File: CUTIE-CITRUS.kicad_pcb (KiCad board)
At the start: 2 copper layers, 85 x 85 mm, 65 parts, among them J1 F32Q-1A7H1-11022, J2 F32Q-1A7H1-11022, J3 Bus_M.2_Socket_M, J4 Hirose U.FL, U1 AP3441SHE-7B, U2 ASEK-32.768KHZ-L-R-T, U3 ICM-42688-P, U4 NEO-M8M

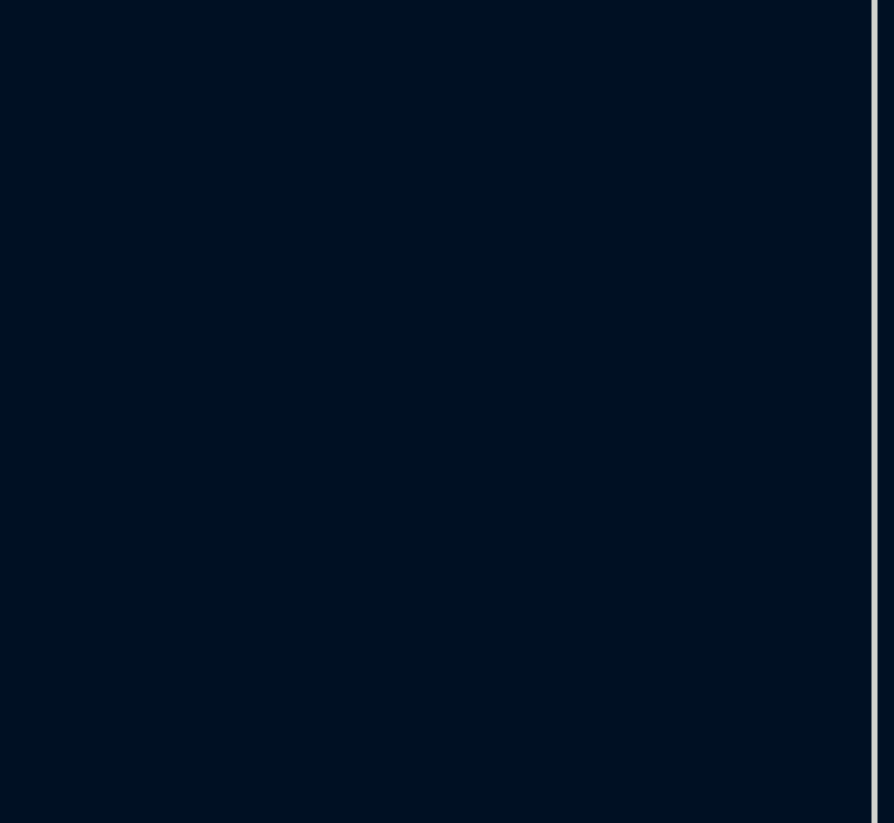
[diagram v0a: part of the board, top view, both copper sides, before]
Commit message: moved TPs
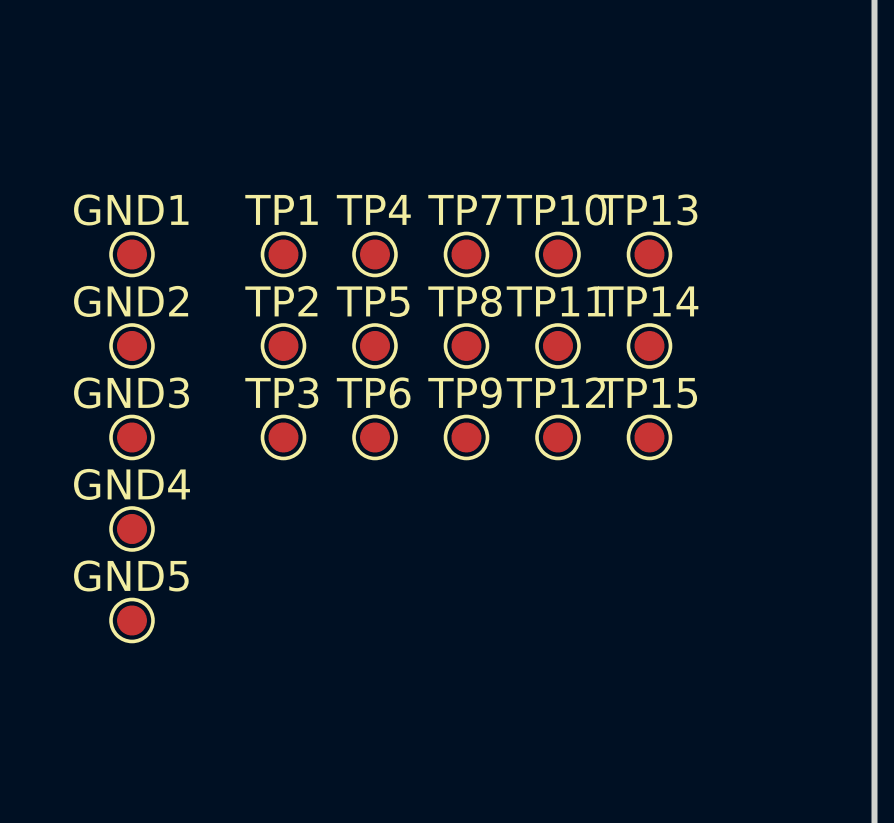
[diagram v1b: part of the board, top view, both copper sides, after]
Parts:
- added GND1: TestPoint, TestPoint:TestPoint_Pad_D1.0mm, F.Cu at (125.2, 96.4)
- added GND2: TestPoint, TestPoint:TestPoint_Pad_D1.0mm, F.Cu at (125.2, 99.5)
- added GND3: TestPoint, TestPoint:TestPoint_Pad_D1.0mm, F.Cu at (125.2, 102.5)
- added GND4: TestPoint, TestPoint:TestPoint_Pad_D1.0mm, F.Cu at (125.2, 105.5)
- added GND5: TestPoint, TestPoint:TestPoint_Pad_D1.0mm, F.Cu at (125.2, 108.6)
- added TP1: TestPoint, TestPoint:TestPoint_Pad_D1.0mm, F.Cu at (130.3, 96.4)
- added TP10: TestPoint, TestPoint:TestPoint_Pad_D1.0mm, F.Cu at (139.4, 96.4)
- added TP11: TestPoint, TestPoint:TestPoint_Pad_D1.0mm, F.Cu at (139.4, 99.5)
- added TP12: TestPoint, TestPoint:TestPoint_Pad_D1.0mm, F.Cu at (139.4, 102.5)
- added TP13: TestPoint, TestPoint:TestPoint_Pad_D1.0mm, F.Cu at (142.5, 96.4)
- added TP14: TestPoint, TestPoint:TestPoint_Pad_D1.0mm, F.Cu at (142.5, 99.5)
- added TP15: TestPoint, TestPoint:TestPoint_Pad_D1.0mm, F.Cu at (142.5, 102.5)
- added TP2: TestPoint, TestPoint:TestPoint_Pad_D1.0mm, F.Cu at (130.3, 99.5)
- added TP3: TestPoint, TestPoint:TestPoint_Pad_D1.0mm, F.Cu at (130.3, 102.5)
- added TP4: TestPoint, TestPoint:TestPoint_Pad_D1.0mm, F.Cu at (133.3, 96.4)
- added TP5: TestPoint, TestPoint:TestPoint_Pad_D1.0mm, F.Cu at (133.3, 99.5)
- added TP6: TestPoint, TestPoint:TestPoint_Pad_D1.0mm, F.Cu at (133.3, 102.5)
- added TP7: TestPoint, TestPoint:TestPoint_Pad_D1.0mm, F.Cu at (136.4, 96.4)
- added TP8: TestPoint, TestPoint:TestPoint_Pad_D1.0mm, F.Cu at (136.4, 99.5)
- added TP9: TestPoint, TestPoint:TestPoint_Pad_D1.0mm, F.Cu at (136.4, 102.5)
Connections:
- net /Sensors/RF_UBLOX renamed /Sensors/RF_GPS
- CM5-1 pad 102: /PCIEsb.nCLKREQ -> /CM5/PCIEsb.nCLKREQ
- CM5-1 pad 104: /PCIEsb.nWAKE -> /CM5/PCIEsb.nWAKE
- CM5-1 pad 106: /PCIEsb.PWR_EN -> /CM5/PCIEsb.PWR_EN
- CM5-1 pad 109: /PCIEsb.nRST -> /CM5/PCIEsb.nRST
- CM5-1 pad 34: /I2C2.SCL -> /CM5/I2C2.SCL
- CM5-1 pad 35: /I2C1.SCL -> /CM5/I2C1.SCL
- CM5-1 pad 36: /I2C1.SDA -> /CM5/I2C1.SDA
- CM5-1 pad 37: /SPI0.CS1n -> /CM5/SPI0.CS1n
- CM5-1 pad 38: /SPI0.SCLK -> /CM5/SPI0.SCLK
- CM5-1 pad 39: /SPI0.CS0n -> /CM5/SPI0.CS0n
- CM5-1 pad 40: /SPI0.MISO -> /CM5/SPI0.MISO
- CM5-1 pad 44: /SPI0.MOSI -> /CM5/SPI0.MOSI
- CM5-1 pad 54: /I2C2.SDA -> /CM5/I2C2.SDA
- CM5-1 pad 80: /I2C0.SCL -> /CM5/I2C0.SCL
- CM5-1 pad 82: /I2C0.SDA -> /CM5/I2C0.SDA
- J1 pad 20: /I2C0.SCL -> /CM5/I2C0.SCL
- J1 pad 21: /I2C0.SDA -> /CM5/I2C0.SDA
- J2 pad 20: /I2C1.SCL -> /CM5/I2C1.SCL
- J2 pad 21: /I2C1.SDA -> /CM5/I2C1.SDA
- J3 pad 50: /PCIEsb.nRST -> /CM5/PCIEsb.nRST
- J3 pad 52: /PCIEsb.nCLKREQ -> /CM5/PCIEsb.nCLKREQ
- J3 pad 54: /PCIEsb.nWAKE -> /CM5/PCIEsb.nWAKE
- R1 pad 2: /I2C1.SDA -> /CM5/I2C1.SDA
- R10 pad 2: /I2C2.SCL -> /CM5/I2C2.SCL
- R11 pad 2: /I2C0.SDA -> /CM5/I2C0.SDA
- R12 pad 2: /I2C0.SCL -> /CM5/I2C0.SCL
- R2 pad 2: /I2C1.SCL -> /CM5/I2C1.SCL
- R5 pad 1: /PCIEsb.PWR_EN -> /CM5/PCIEsb.PWR_EN
- R9 pad 2: /I2C2.SDA -> /CM5/I2C2.SDA
- U1 pad 7: /PCIEsb.PWR_EN -> /CM5/PCIEsb.PWR_EN
- U3 pad 1: /SPI0.MISO -> /CM5/SPI0.MISO
- U3 pad 12: /SPI0.CS0n -> /CM5/SPI0.CS0n
- U3 pad 13: /SPI0.SCLK -> /CM5/SPI0.SCLK
- U3 pad 14: /SPI0.MOSI -> /CM5/SPI0.MOSI
- U4 pad 18: /SPI0.CS1n -> /CM5/SPI0.CS1n
- U4 pad 19: /SPI0.SCLK -> /CM5/SPI0.SCLK
- U4 pad 20: /SPI0.MISO -> /CM5/SPI0.MISO
- U4 pad 21: /SPI0.MOSI -> /CM5/SPI0.MOSI

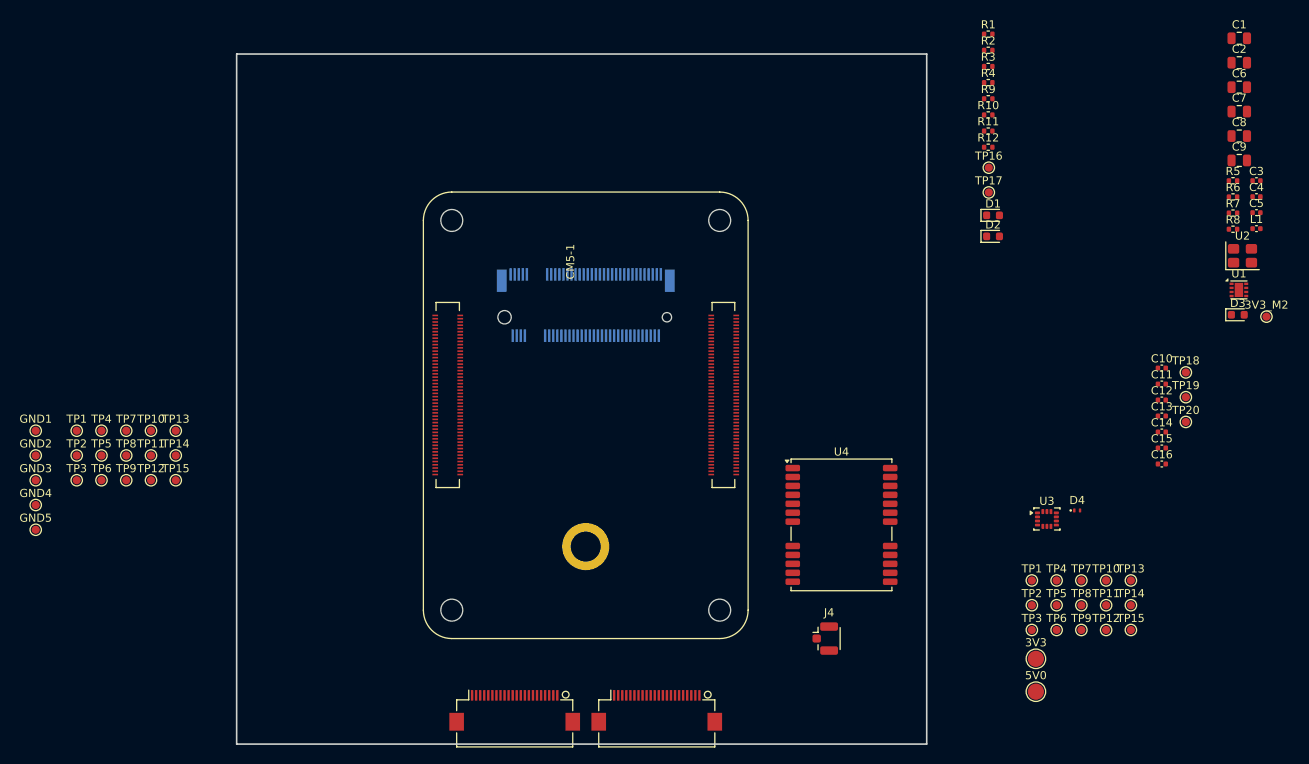
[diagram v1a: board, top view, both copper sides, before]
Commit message: added temp sensors
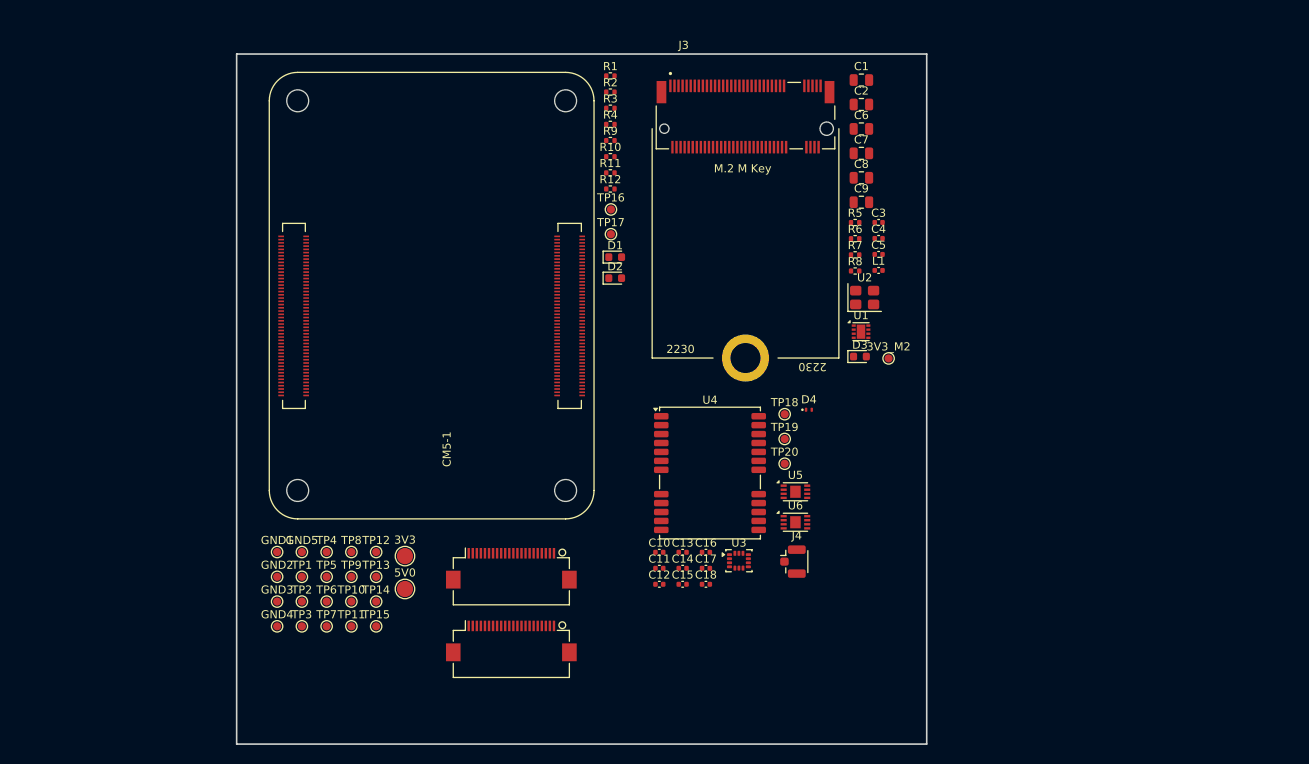
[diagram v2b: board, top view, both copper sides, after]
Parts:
- removed the TP1 at (247.9, 114.8)
- removed the TP1 at (130.3, 96.4)
- removed the TP10 at (257.1, 114.8)
- removed the TP10 at (139.4, 96.4)
- removed the TP11 at (139.4, 99.5)
- removed the TP11 at (257.1, 117.9)
- removed the TP12 at (139.4, 102.5)
- removed the TP12 at (257.1, 120.9)
- removed the TP13 at (260.1, 114.8)
- removed the TP13 at (142.5, 96.4)
- removed the TP14 at (142.5, 99.5)
- removed the TP14 at (260.1, 117.9)
- removed the TP15 at (142.5, 102.5)
- removed the TP15 at (260.1, 120.9)
- removed the TP2 at (247.9, 117.9)
- removed the TP2 at (130.3, 99.5)
- removed the TP3 at (247.9, 120.9)
- removed the TP3 at (130.3, 102.5)
- removed the TP4 at (133.3, 96.4)
- removed the TP4 at (251.0, 114.8)
- removed the TP5 at (251.0, 117.9)
- removed the TP5 at (133.3, 99.5)
- removed the TP6 at (133.3, 102.5)
- removed the TP6 at (251.0, 120.9)
- removed the TP7 at (136.4, 96.4)
- removed the TP7 at (254.1, 114.8)
- removed the TP8 at (254.1, 117.9)
- removed the TP8 at (136.4, 99.5)
- removed the TP9 at (254.1, 120.9)
- removed the TP9 at (136.4, 102.5)
- added C17: 0.1uF, Capacitor_SMD:C_0402_1005Metric, F.Cu at (207.8, 113.3)
- added C18: 0.1uF, Capacitor_SMD:C_0402_1005Metric, F.Cu at (207.8, 115.3)
- added TP1: TestPoint, TestPoint:TestPoint_Pad_D1.0mm, F.Cu at (158.0, 114.4)
- added TP10: TestPoint, TestPoint:TestPoint_Pad_D1.0mm, F.Cu at (164.1, 117.4)
- added TP11: TestPoint, TestPoint:TestPoint_Pad_D1.0mm, F.Cu at (164.1, 120.5)
- added TP12: TestPoint, TestPoint:TestPoint_Pad_D1.0mm, F.Cu at (167.2, 111.3)
- added TP13: TestPoint, TestPoint:TestPoint_Pad_D1.0mm, F.Cu at (167.2, 114.4)
- added TP14: TestPoint, TestPoint:TestPoint_Pad_D1.0mm, F.Cu at (167.2, 117.4)
- added TP15: TestPoint, TestPoint:TestPoint_Pad_D1.0mm, F.Cu at (167.2, 120.5)
- added TP2: TestPoint, TestPoint:TestPoint_Pad_D1.0mm, F.Cu at (158.0, 117.4)
- added TP3: TestPoint, TestPoint:TestPoint_Pad_D1.0mm, F.Cu at (158.0, 120.5)
- added TP4: TestPoint, TestPoint:TestPoint_Pad_D1.0mm, F.Cu at (161.1, 111.3)
- added TP5: TestPoint, TestPoint:TestPoint_Pad_D1.0mm, F.Cu at (161.1, 114.4)
- added TP6: TestPoint, TestPoint:TestPoint_Pad_D1.0mm, F.Cu at (161.1, 117.4)
- added TP7: TestPoint, TestPoint:TestPoint_Pad_D1.0mm, F.Cu at (161.1, 120.5)
- added TP8: TestPoint, TestPoint:TestPoint_Pad_D1.0mm, F.Cu at (164.1, 111.3)
- added TP9: TestPoint, TestPoint:TestPoint_Pad_D1.0mm, F.Cu at (164.1, 114.4)
- added U5: MCP98243, Package_DFN_QFN:DFN-8-1EP_3x2mm_P0.5mm_EP1.3x1.5mm, F.Cu at (218.8, 103.9)
- added U6: MCP98243, Package_DFN_QFN:DFN-8-1EP_3x2mm_P0.5mm_EP1.3x1.5mm, F.Cu at (218.8, 107.7)
- J3: moved to F.Cu
- moved 3V3 78.7 mm to (170.7, 111.8)
- moved 5V0 78.7 mm to (170.7, 115.9)
- moved C10 65.9 mm to (202.1, 111.4)
- moved C11 65.9 mm to (202.1, 113.3)
- moved C12 65.9 mm to (202.1, 115.3)
- moved CM5-1 61.7 mm to (157.5, 103.8), turned to 0 degrees
- moved C13 61.4 mm to (204.9, 111.4)
- moved C14 61.4 mm to (204.9, 113.3)
- moved C15 61.4 mm to (204.9, 115.3)
- moved C16 57.2 mm to (207.8, 111.4)
- moved TP18 49.7 mm to (217.5, 94.4)
- moved TP19 49.7 mm to (217.5, 97.4)
- moved TP20 49.7 mm to (217.5, 100.5)
- moved 3V3_M2 46.8 mm to (230.3, 87.5)
- moved C3 46.8 mm to (229.1, 70.7)
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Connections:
- net /3V3 renamed /Cameras/3V3
- net /5V0 renamed /Backplane Connector/5V0

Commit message: added potential backplane conn
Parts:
- added REF**: SAMTEC_ERM8-025-XX-X-D-RA-XX, library:SAMTEC_ERM8-025-XX-X-D-RA-XX, F.Cu at (216.5, 131.5)

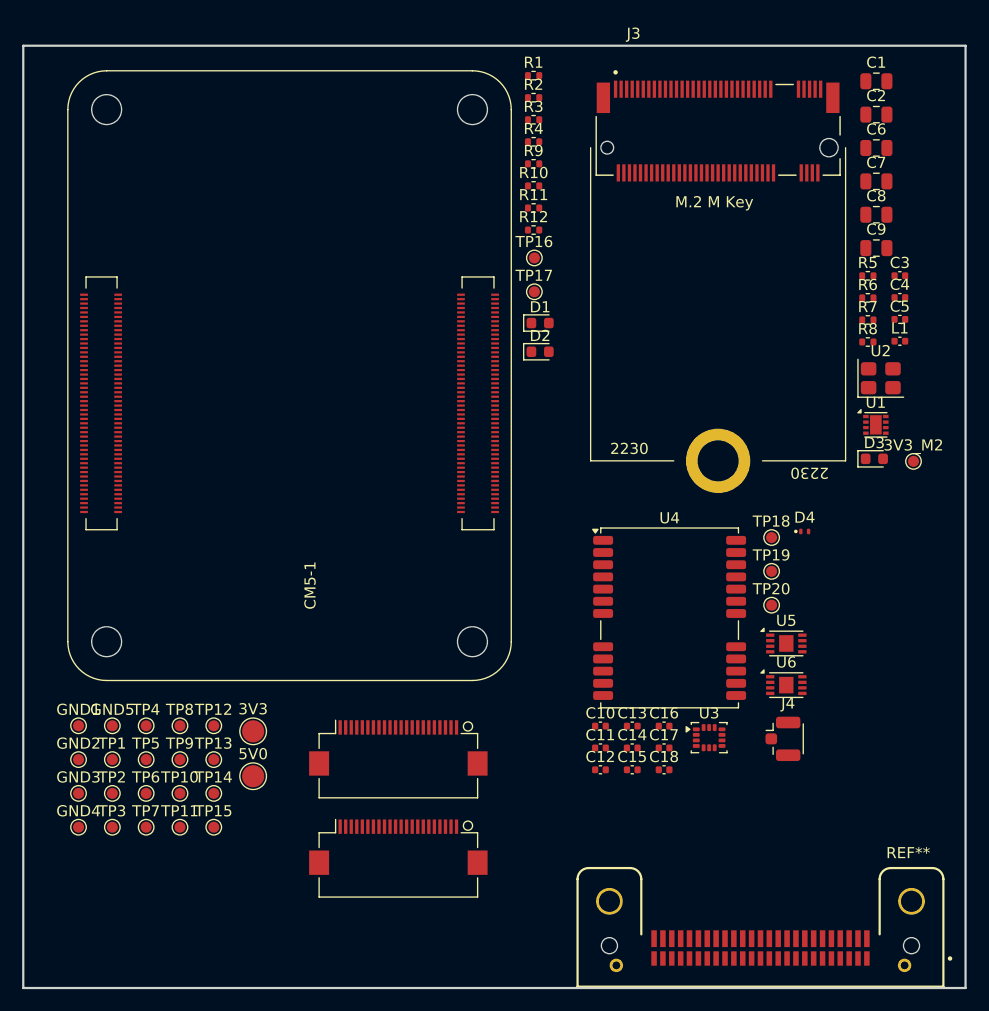
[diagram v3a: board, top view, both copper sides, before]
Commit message: added conns to backplane
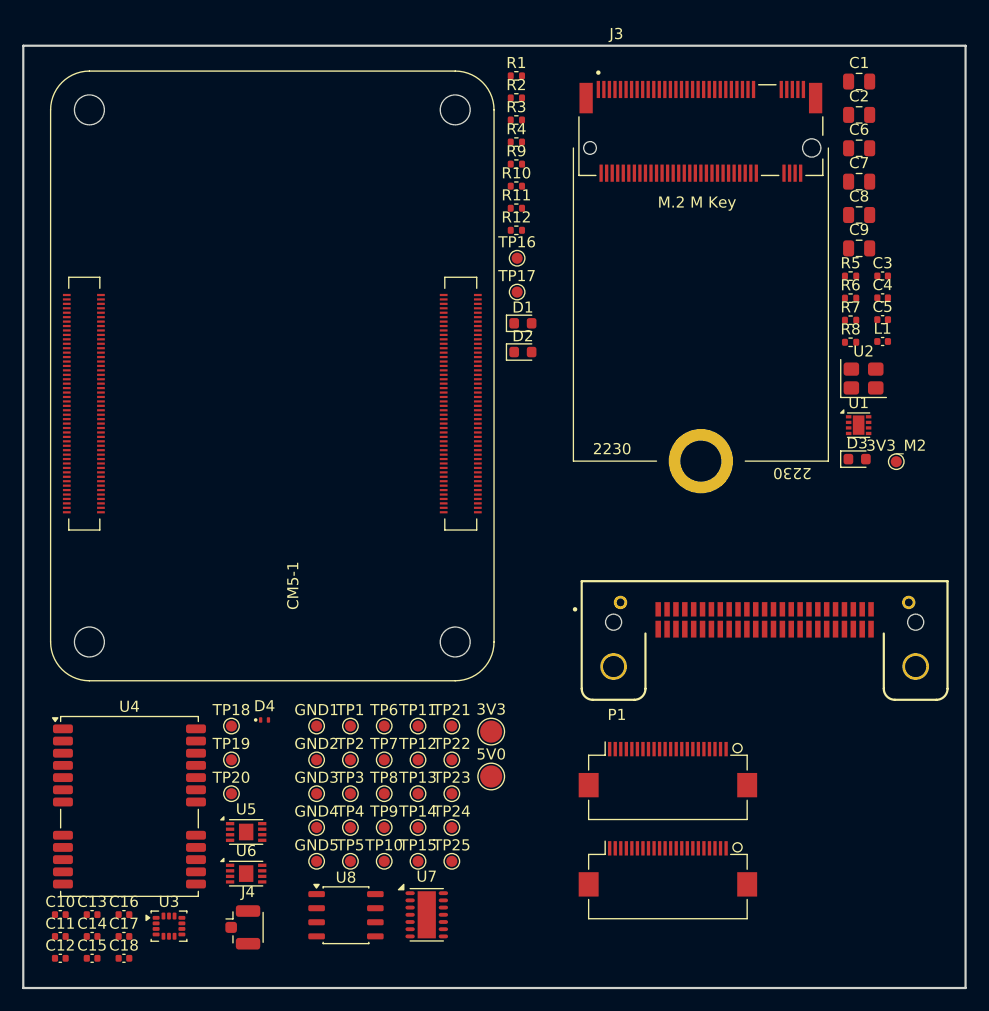
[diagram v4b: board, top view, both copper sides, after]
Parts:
- removed REF**: SAMTEC_ERM8-025-XX-X-D-RA-XX, library:SAMTEC_ERM8-025-XX-X-D-RA-XX
- added P1: ERM8-025-01-L-D-RA-K-TR, library:SAMTEC_ERM8-025-XX-X-D-RA-XX, F.Cu at (216.9, 101.7)
- added TP21: TestPoint, TestPoint:TestPoint_Pad_D1.0mm, F.Cu at (188.7, 111.4)
- added TP22: TestPoint, TestPoint:TestPoint_Pad_D1.0mm, F.Cu at (188.7, 114.4)
- added TP23: TestPoint, TestPoint:TestPoint_Pad_D1.0mm, F.Cu at (188.7, 117.5)
- added TP24: TestPoint, TestPoint:TestPoint_Pad_D1.0mm, F.Cu at (188.7, 120.5)
- added TP25: TestPoint, TestPoint:TestPoint_Pad_D1.0mm, F.Cu at (188.7, 123.6)
- added U7: MCP2518FD-xQBB, Package_DFN_QFN:DFN-14-1EP_3x4.5mm_P0.65mm_EP1.65x4.25mm, F.Cu at (186.4, 128.4)
- added U8: TCAN334, Package_SO:JEITA_SOIC-8_3.9x4.9mm_P1.27mm, F.Cu at (179.1, 128.4)
- moved D4 51.6 mm to (171.8, 110.8)
- moved U5 51.6 mm to (170.1, 120.9)
- moved U6 51.6 mm to (170.1, 124.7)
- moved TP18 51.6 mm to (168.8, 111.4)
- moved U4 51.6 mm to (159.6, 118.6)
- moved C10 51.6 mm to (153.3, 128.4)
- moved C11 51.6 mm to (153.3, 130.3)
- moved C12 51.6 mm to (153.3, 132.3)
- moved C13 51.6 mm to (156.2, 128.4)
- moved C14 51.6 mm to (156.2, 130.3)
- moved C15 51.6 mm to (156.2, 132.3)
- moved C16 51.6 mm to (159.1, 128.4)
- moved C17 51.6 mm to (159.1, 130.3)
- moved C18 51.6 mm to (159.1, 132.3)
- moved J4 51.6 mm to (169.8, 129.5)
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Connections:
- net /CM5/USB3.D_N renamed /Backplane Connector/USB3.D_N
- net /CM5/USB3.D_P renamed /Backplane Connector/USB3.D_P
- CM5-1 pad 157: /CM5/USB3.RX_N -> /Backplane Connector/USB3.RX_N
- CM5-1 pad 159: /CM5/USB3.RX_P -> /Backplane Connector/USB3.RX_P
- CM5-1 pad 169: /CM5/USB3.TX_N -> /Backplane Connector/USB3.TX_N
- CM5-1 pad 171: /CM5/USB3.TX_P -> /Backplane Connector/USB3.TX_P
